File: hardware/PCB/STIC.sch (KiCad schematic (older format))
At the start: 12 parts, among them J1 DIP-JST-2P-2.0, J2 Button connector, J3 Laser A, J4 Laser B, Q1 Q_PMOS_GSD, U1 XIAO_BLE, U2 RM3100_Breakout, U3 MDOB048064AV

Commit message: update hardware files, note Button and main board are not connected proper
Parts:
- LS1: footprint Buzzer_Beeper:Buzzer_D14mm_H7mm_P10mm -> Buzzer_Beeper:Buzzer_15x7.5RM7.6
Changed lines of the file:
@@
 F 0 "LS1" H 2863 1933 50  0000 C CNN
 F 1 "Speaker" H 2863 2024 50  0000 C CNN
-F 2 "Buzzer_Beeper:Buzzer_D14mm_H7mm_P10mm" H 2900 2150 50  0001 C CNN
+F 2 "Buzzer_Beeper:Buzzer_15x7.5RM7.6" H 2900 2150 50  0001 C CNN
 F 3 "~" H 2890 2300 50  0001 C CNN
 	1    2900 2350

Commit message: Fix error in order of pins on button PCB, and other minor PCB fixes
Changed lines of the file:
@@
 Text Label 8550 2250 2    50   ~ 0
 BUTTON
+Text Label 5900 3400 0    50   ~ 0
+LED2_R
 Text Label 3500 3100 2    50   ~ 0
-LED2_R
-Text Label 5900 3400 0    50   ~ 0
 LED2_G
 Text Label 5900 3250 0    50   ~ 0
@@
 Wire Wire Line
 	8750 2550 8550 2550
+Text Label 8550 2450 2    50   ~ 0
+LED2_R
 Text Label 8550 2350 2    50   ~ 0
-LED2_R
-Text Label 8550 2450 2    50   ~ 0
 LED2_G
 Text Label 8550 2550 2    50   ~ 0

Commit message: Convert main pcb to work with egismos laser
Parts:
- removed J1: DIP-JST-2P-2.0, Connector_JST:JST_PH_S2B-PH-K_1x02_P2.00mm_Horizontal, symbol OPL_Connector:DIP-JST-2P-2.0
- removed J2: Button connector, Connector_PinHeader_2.54mm:PinHeader_1x06_P2.54mm_Vertical, symbol Connector_Generic:Conn_01x06
- removed J3: Laser A, Connector_Wuerth:Wuerth_WR-WTB_64800611622_1x06_P1.50mm_Vertical, symbol Connector_Generic:Conn_01x06
- removed J4: Laser B, Connector_Wuerth:Wuerth_WR-WTB_64800811622_1x08_P1.50mm_Vertical, symbol Connector_Generic:Conn_01x08
- removed Q1: Q_PMOS_GSD, Package_TO_SOT_SMD:TSOT-23_HandSoldering, symbol Device:Q_PMOS_GSD
- added C1: 1uF, Capacitor_THT:C_Rect_L7.2mm_W2.5mm_P5.00mm_FKS2_FKP2_MKS2_MKP2, symbol Device:CP
- added C2: 47uF, Capacitor_THT:C_Rect_L7.2mm_W5.5mm_P5.00mm_FKS2_FKP2_MKS2_MKP2, symbol Device:CP
- added IC1: NCP59301DS33R4G, Package_TO_SOT_SMD:TO-263-5_TabPin6, symbol SamacSys:NCP59301DS33R4G
- added J1: 22-03-5035, Connector_Molex:Molex_SPOX_5267-03A_1x03_P2.50mm_Vertical, symbol SamacSys:22-03-5035
- added J2: 53047-0510, Connector_Molex:Molex_PicoBlade_53047-0510_1x05_P1.25mm_Vertical, symbol SamacSys:53047-0510
- added J3: 53047-0310, Connector_Molex:Molex_PicoBlade_53047-0310_1x03_P1.25mm_Vertical, symbol SamacSys:53047-0310
- LS1: footprint Buzzer_Beeper:Buzzer_15x7.5RM7.6 -> KiCad_imports:SPKR_AST1240MLTRQ
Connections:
- net labels added: BUTTON_A, BUTTON_B, BUZZER_A, BUZZER_B, DRDY, LASER_EN
- net labels removed: +3.3VA, BUTTON, LED2_B, LED2_G, LED2_R
- wire segments 63 -> 73
- no-connect marks 17 -> 9
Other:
- moved on the sheet: LS1, R1

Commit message: Update board to show new display, and minor tidying on button board
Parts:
- removed U3: MDOB048064AV, KiCad_imports:MDOB048064AV, symbol MDOB048064AV:MDOB048064AV
- added U3: MDOB128064XV, KiCad_imports:MDOB128064XV, symbol MDOB048064AV:MDOB128064XV
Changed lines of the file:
@@
-	1    0    0    -1
-$EndComp
-$Comp
-L MDOB048064AV:MDOB048064AV U3
-U 1 1 63C9E2F3
-P 4300 5500
-F 0 "U3" H 3973 5546 50  0000 R CNN
-F 1 "MDOB048064AV" H 3973 5455 50  0000 R CNN
-F 2 "KiCad_imports:MDOB048064AV" H 4300 5500 50  0001 C CNN
-F 3 "" H 4300 5500 50  0001 C CNN
-	1    4300 5500
 	1    0    0    -1
 $EndComp
@@
 Wire Wire Line
 	7750 3950 7050 3950
+$Comp
+L MDOB048064AV:MDOB128064XV U3
+U 1 1 641687AF
+P 4300 5500
+F 0 "U3" H 3972 5546 50  0000 R CNN
+F 1 "MDOB128064XV" H 3972 5455 50  0000 R CNN
+F 2 "KiCad_imports:MDOB128064XV" H 4300 5500 50  0001 C CNN
+F 3 "" H 4300 5500 50  0001 C CNN
+	1    4300 5500
+	1    0    0    -1
+$EndComp
 $EndSCHEMATC

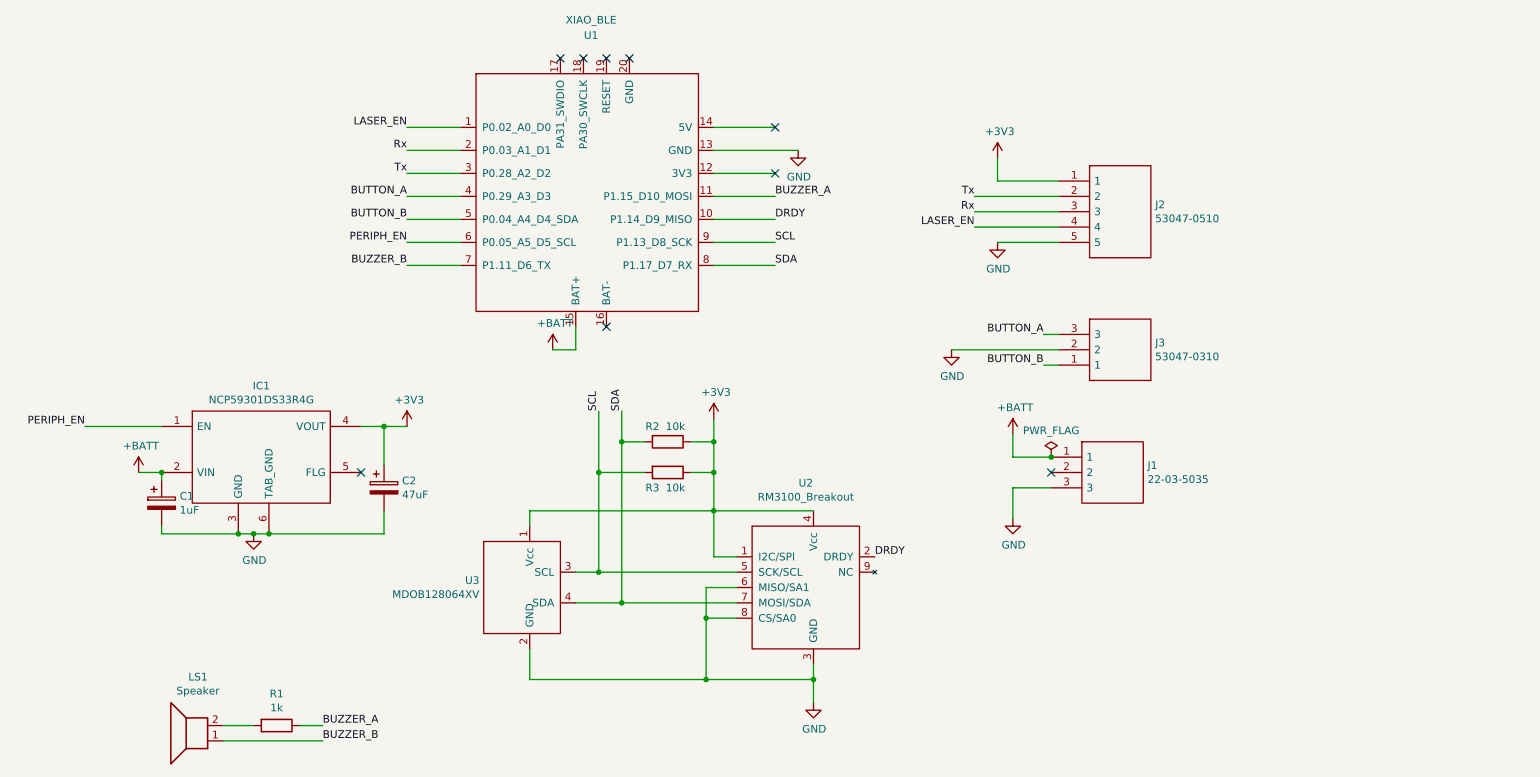
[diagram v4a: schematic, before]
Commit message: Add battery charger IC and switch caps to SMT tech
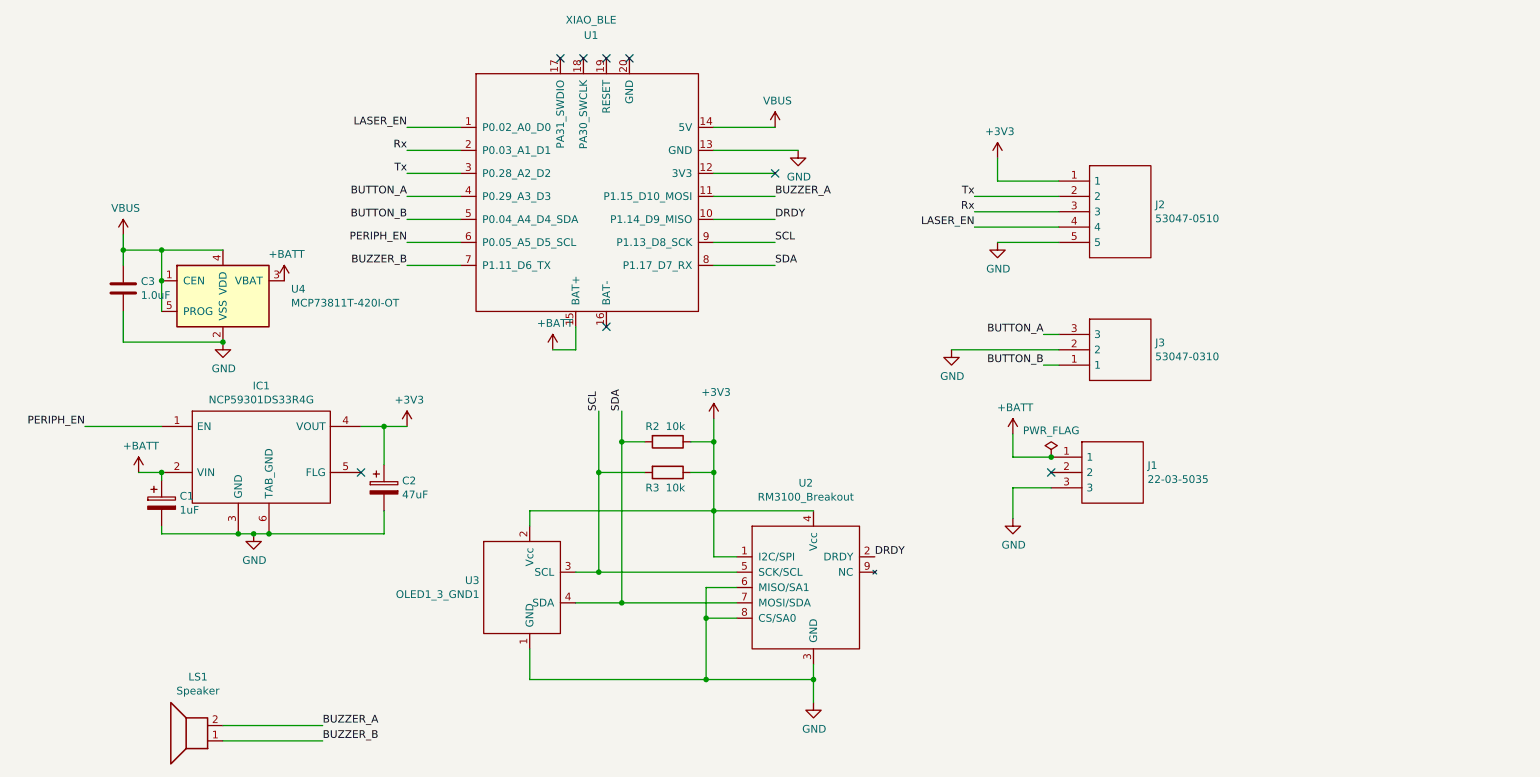
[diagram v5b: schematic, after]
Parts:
- removed R1: 1k, Resistor_THT:R_Axial_DIN0207_L6.3mm_D2.5mm_P7.62mm_Horizontal, symbol Device:R
- removed U3: MDOB128064XV, KiCad_imports:MDOB128064XV, symbol MDOB048064AV:MDOB128064XV
- added C3: 1.0uF, Capacitor_SMD:C_1210_3225Metric_Pad1.42x2.65mm_HandSolder, symbol Device:C
- added U3: OLED1_3_GND1, KiCad_imports:OLED1_3, symbol MDOB048064AV:OLED1_3_GND1
- added U4: MCP73811T-420I-OT, Package_TO_SOT_SMD:SOT-23-5, symbol Battery_Management:MCP73811T-420I-OT
- C1: footprint Capacitor_THT:C_Rect_L7.2mm_W2.5mm_P5.00mm_FKS2_FKP2_MKS2_MKP2 -> Capacitor_SMD:C_1210_3225Metric_Pad1.42x2.65mm_HandSolder
- C2: footprint Capacitor_THT:C_Rect_L7.2mm_W5.5mm_P5.00mm_FKS2_FKP2_MKS2_MKP2 -> Capacitor_SMD:C_1210_3225Metric
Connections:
- net +3V3: now also U3.2 (Vcc)
- net +BATT: now also U4.3 (VBAT)
- net BUZZER_A: now also LS1.2
- net GND: now also C3.2, U3.1 (GND), U4.2 (VSS)
- net SCL: now also U3.3 (SCL)
- net SDA: now also U3.4 (SDA)
- net VBUS: now reaches U1.14 (5V)
- net VBUS: now also C3.1, U4.1 (CEN), U4.4 (VDD), U4.5 (PROG)
- no-connect marks 9 -> 8
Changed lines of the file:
@@
 Text Label 3500 2650 2    50   ~ 0
 Rx
-NoConn ~ 5900 2500
 Wire Wire Line
 	5500 2650 6050 2650
@@
 Wire Wire Line
 	4600 3800 4600 3950
-$Comp
-L Device:R R1
-U 1 1 6354E502
-P 2650 6400
-F 0 "R1" V 2443 6400 50  0000 C CNN
-F 1 "1k" V 2534 6400 50  0000 C CNN
-F 2 "Resistor_THT:R_Axial_DIN0207_L6.3mm_D2.5mm_P7.62mm_Horizontal" V 2580 6400 50  0001 C CNN
-F 3 "~" H 2650 6400 50  0001 C CNN
-	1    2650 6400
-	0    1    1    0
-$EndComp
-Wire Wire Line
-	2950 6400 2800 6400
-Wire Wire Line
-	2500 6400 2300 6400
+Wire Wire Line
+	2950 6400 2300 6400
 Text Label 4750 4350 1    50   ~ 0
 SCL
@@
 F 0 "C2" H 3468 4896 50  0000 L CNN
 F 1 "47uF" H 3468 4805 50  0000 L CNN
-F 2 "Capacitor_THT:C_Rect_L7.2mm_W5.5mm_P5.00mm_FKS2_FKP2_MKS2_MKP2" H 3388 4700 50  0001 C CNN
+F 2 "Capacitor_SMD:C_1210_3225Metric" H 3388 4700 50  0001 C CNN
 F 3 "~" H 3350 4850 50  0001 C CNN
 	1    3350 4850
@@
 F 0 "C1" H 2018 4996 50  0000 L CNN
 F 1 "1uF" H 2018 4905 50  0000 L CNN
-F 2 "Capacitor_THT:C_Rect_L7.2mm_W2.5mm_P5.00mm_FKS2_FKP2_MKS2_MKP2" H 1938 4800 50  0001 C CNN
+F 2 "Capacitor_SMD:C_1210_3225Metric_Pad1.42x2.65mm_HandSolder" H 1938 4800 50  0001 C CNN
 F 3 "~" H 1900 4950 50  0001 C CNN
 	1    1900 4950
@@
 	7750 3950 7050 3950
 $Comp
-L MDOB048064AV:MDOB128064XV U3
-U 1 1 641687AF
+L MDOB048064AV:OLED1_3_GND1 U3
+U 1 1 641F20DC
 P 4300 5500
 F 0 "U3" H 3972 5546 50  0000 R CNN
-F 1 "MDOB128064XV" H 3972 5455 50  0000 R CNN
-F 2 "KiCad_imports:MDOB128064XV" H 4300 5500 50  0001 C CNN
+F 1 "OLED1_3_GND1" H 3972 5455 50  0000 R CNN
+F 2 "KiCad_imports:OLED1_3" H 4300 5500 50  0001 C CNN
 F 3 "" H 4300 5500 50  0001 C CNN
 	1    4300 5500
 	1    0    0    -1
 $EndComp
+$Comp
+L power:VBUS #PWR0110
+U 1 1 6459D153
+P 5900 2500
+F 0 "#PWR0110" H 5900 2350 50  0001 C CNN
+F 1 "VBUS" H 5915 2673 50  0000 C CNN
+F 2 "" H 5900 2500 50  0001 C CNN
+F 3 "" H 5900 2500 50  0001 C CNN
+	1    5900 2500
+	1    0    0    -1
+$EndComp
+$Comp
+L Battery_Management:MCP73811T-420I-OT U4
+U 1 1 645AAEDE
+P 2300 3600
+F 0 "U4" H 2744 3646 50  0000 L CNN
+F 1 "MCP73811T-420I-OT" H 2744 3555 50  0000 L CNN
+F 2 "Package_TO_SOT_SMD:SOT-23-5" H 2350 3350 50  0001 L CNN
+F 3 "http://ww1.microchip.com/downloads/en/DeviceDoc/22036b.pdf" H 2050 3850 50  0001 C CNN
+	1    2300 3600
+	1    0    0    -1
+$EndComp
+$Comp
+L power:VBUS #PWR0111
+U 1 1 645AB5C7
+P 1650 3200
+F 0 "#PWR0111" H 1650 3050 50  0001 C CNN
+F 1 "VBUS" H 1665 3373 50  0000 C CNN
+F 2 "" H 1650 3200 50  0001 C CNN
+F 3 "" H 1650 3200 50  0001 C CNN
+	1    1650 3200
+	1    0    0    -1
+$EndComp
+Wire Wire Line
+	1650 3200 1650 3300
+Wire Wire Line
+	1650 3300 1900 3300
+Wire Wire Line
+	1900 3300 1900 3500
+Connection ~ 1900 3500
+Wire Wire Line
+	1900 3500 1900 3700
+Wire Wire Line
+	1900 3300 2300 3300
+Connection ~ 1900 3300
+$Comp
+L power:GND #PWR0112
+U 1 1 645AF8C2
+P 2300 3900
+F 0 "#PWR0112" H 2300 3650 50  0001 C CNN
+F 1 "GND" H 2305 3727 50  0000 C CNN
+F 2 "" H 2300 3900 50  0001 C CNN
+F 3 "" H 2300 3900 50  0001 C CNN
+	1    2300 3900
+	1    0    0    -1
+$EndComp
+$Comp
+L power:+BATT #PWR0113
+U 1 1 645AFD74
+P 2700 3500
+F 0 "#PWR0113" H 2700 3350 50  0001 C CNN
+F 1 "+BATT" H 2715 3673 50  0000 C CNN
+F 2 "" H 2700 3500 50  0001 C CNN
+F 3 "" H 2700 3500 50  0001 C CNN
+	1    2700 3500
+	1    0    0    -1
+$EndComp
+Connection ~ 1650 3300
+$Comp
+L Device:C C3
+U 1 1 645B2C07
+P 1650 3550
+F 0 "C3" H 1765 3596 50  0000 L CNN
+F 1 "1.0uF" H 1765 3505 50  0000 L CNN
+F 2 "Capacitor_SMD:C_1210_3225Metric_Pad1.42x2.65mm_HandSolder" H 1688 3400 50  0001 C CNN
+F 3 "~" H 1650 3550 50  0001 C CNN
+	1    1650 3550
+	1    0    0    -1
+$EndComp
+Wire Wire Line
+	2300 3900 1650 3900
+Wire Wire Line
+	1650 3900 1650 3700
+Connection ~ 2300 3900
+Wire Wire Line
+	1650 3300 1650 3400
 $EndSCHEMATC

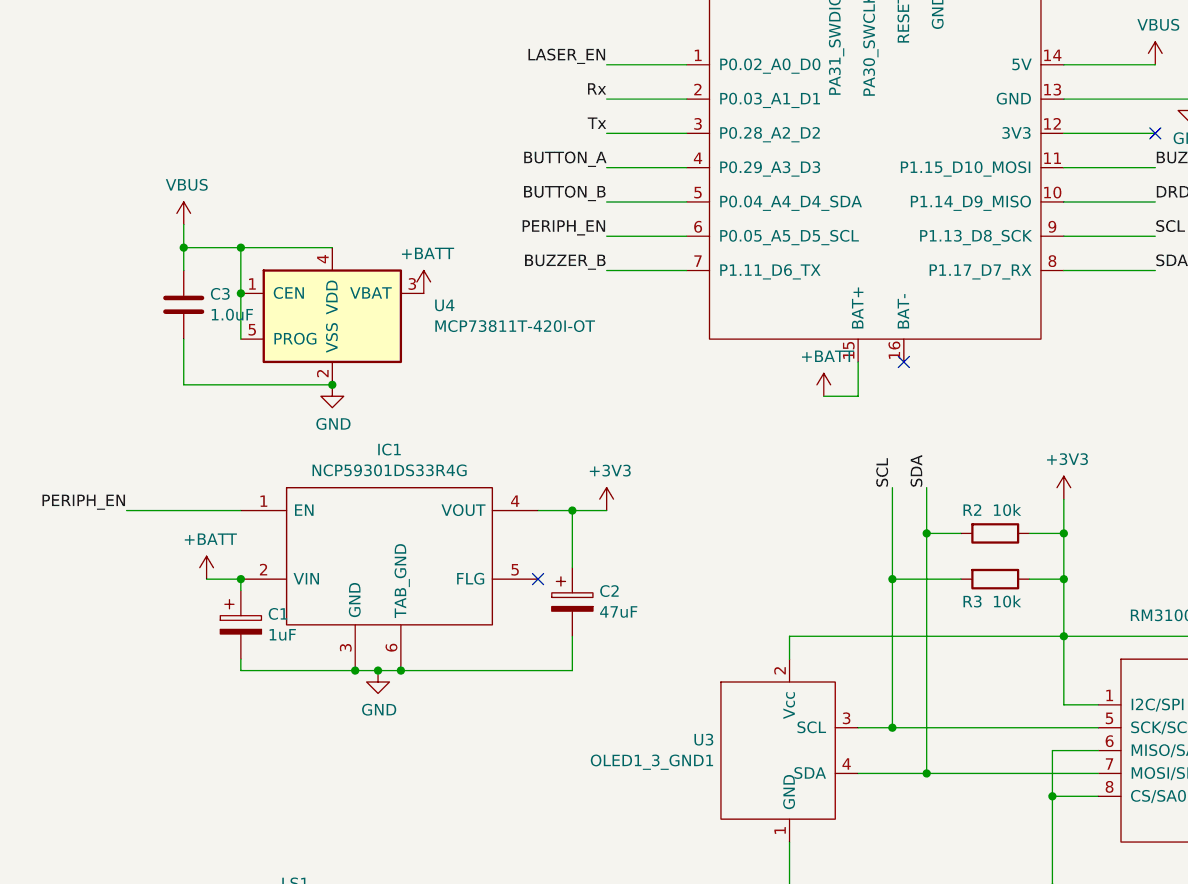
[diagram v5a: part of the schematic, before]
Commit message: Update pcb to include battery charging and smaller current controller
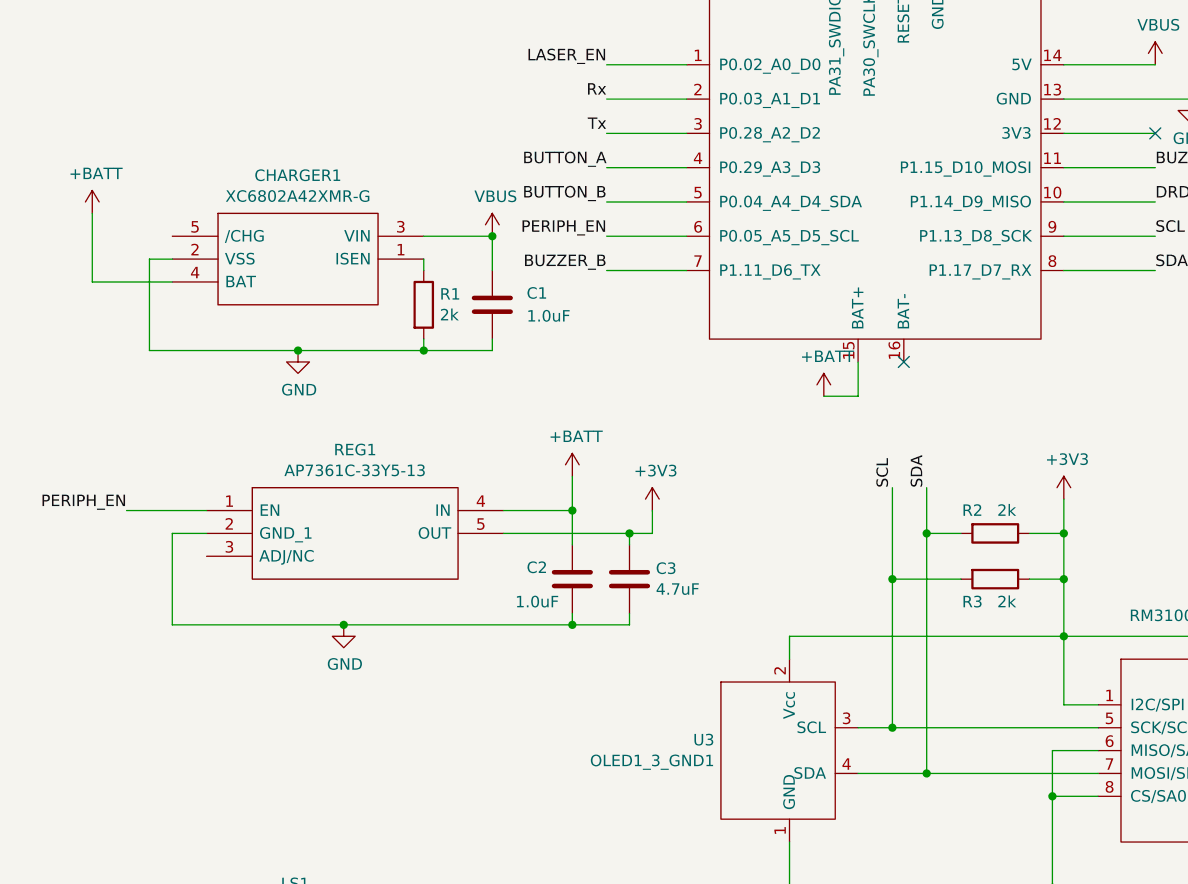
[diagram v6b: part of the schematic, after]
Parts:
- removed C1: 1uF, Capacitor_SMD:C_1210_3225Metric_Pad1.42x2.65mm_HandSolder, symbol Device:CP
- removed C2: 47uF, Capacitor_SMD:C_1210_3225Metric, symbol Device:CP
- removed IC1: NCP59301DS33R4G, Package_TO_SOT_SMD:TO-263-5_TabPin6, symbol SamacSys:NCP59301DS33R4G
- removed U4: MCP73811T-420I-OT, Package_TO_SOT_SMD:SOT-23-5, symbol Battery_Management:MCP73811T-420I-OT
- added C1, C2: 1.0uF, Capacitor_THT:C_Disc_D5.0mm_W2.5mm_P2.50mm, symbol Device:C
- added CHARGER1: XC6802A42XMR-G, Package_TO_SOT_SMD:SOT-89-5_Handsoldering, symbol XC6802A42XMR-G:XC6802A42XMR-G
- added R1: 2k, Resistor_THT:R_Axial_DIN0204_L3.6mm_D1.6mm_P5.08mm_Horizontal, symbol Device:R
- added REG1: AP7361C-33Y5-13, Package_TO_SOT_SMD:SOT-89-5_Handsoldering, symbol AP7361C-33Y5-13:AP7361C-33Y5-13
- C3: value 1.0uF -> 4.7uF; footprint Capacitor_SMD:C_1210_3225Metric_Pad1.42x2.65mm_HandSolder -> Capacitor_THT:C_Disc_D5.0mm_W2.5mm_P2.50mm; Farnell Part Number (none) -> 3618969; Manufacturer_Part_Number (none) -> FG14X5R1H475KRT06
- LS1: Manufacturer_Part_Number (none) -> AST1240MLTRQ
- R2, R3: value 10k -> 2k; footprint Resistor_THT:R_Axial_DIN0207_L6.3mm_D2.5mm_P7.62mm_Horizontal -> Resistor_THT:R_Axial_DIN0204_L3.6mm_D1.6mm_P5.08mm_Horizontal; Farnell Part Number (none) -> 9342788; Manufacturer_Part_Number (none) -> MF12 2K
- U1: Farnell Part Number (none) -> 4060352; Manufacturer_Part_Number (none) -> 102010469; Mouser Part Number (none) -> 4060352
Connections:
- net +3V3: now also C3.1, REG1.5 (OUT)
- net +BATT: now also C2.1, CHARGER1.4 (BAT), REG1.4 (IN)
- net GND: now also C1.2, C2.2, CHARGER1.2 (VSS), R1.2, REG1.2 (GND_1)
- net PERIPH_EN: now also REG1.1 (EN)
- net VBUS: now also C1.1, CHARGER1.3 (VIN); no longer C3.1
- new net: CHARGER1.1 (ISEN), R1.1
- no-connect marks 8 -> 7
